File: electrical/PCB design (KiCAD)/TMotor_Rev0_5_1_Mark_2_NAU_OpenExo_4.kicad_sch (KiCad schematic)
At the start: 2 parts

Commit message: documentation update for my 10 days leave ; documentation for first time teensy setup on Arduino IDE ;  SW revamp to use HW versioning conditional compiling
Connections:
- net Left LC  Amplifier 1/Vexcitation+ renamed LEFT_AMP1_EXC
- net Left LC Amplifier 2/Vbridge+ renamed LEFT_AMP2_EXC
- net Right LC  Amplifier 2/Vexcitation+ renamed RIGHT_AMP2_EXC
- net Right LC Amplifier 1/Vexcitation+ renamed RIGHT_AMP1_EXC
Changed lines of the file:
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@@
+		)
+	)
+	(global_label "RIGHT_AMP1_EXC"
+		(shape input)
+		(at 223.52 100.33 0)
+		(fields_autoplaced yes)
+		(effects
+			(font
+				(size 1.27 1.27)
+			)
+			(justify left)
+		)
+		(property "Intersheetrefs" "${INTERSHEET_REFS}"
+			(at 242.5313 100.33 0)
+			(effects
+				(font
+					(size 1.27 1.27)
+				)
+				(justify left)
+				(hide yes)
+			)
 		)
 	)
@@
 		)
 	)
+	(global_label "LEFT_AMP1_EXC"
+		(shape input)
+		(at 120.65 88.9 0)
+		(fields_autoplaced yes)
+		(effects
+			(font
+				(size 1.27 1.27)
+			)
+			(justify left)
+		)
+		(property "Intersheetrefs" "${INTERSHEET_REFS}"
+			(at 138.4517 88.9 0)
+			(effects
+				(font
+					(size 1.27 1.27)
+				)
+				(justify left)
+				(hide yes)
+			)
+		)
+	)
+	(global_label "LEFT_AMP2_EXC"
+		(shape input)
+		(at 118.11 101.6 0)
+		(fields_autoplaced yes)
+		(effects
+			(font
+				(size 1.27 1.27)
+			)
+			(justify left)
+		)
+		(property "Intersheetrefs" "${INTERSHEET_REFS}"
+			(at 135.9117 101.6 0)
+			(effects
+				(font
+					(size 1.27 1.27)
+				)
+				(justify left)
+				(hide yes)
+			)
+		)
+	)
 	(global_label "LEFT_LC_AMP1"
 		(shape input)
@@
 				(hide yes)
 			)
+		)
+	)
+	(global_label "RIGHT_AMP2_EXC"
+		(shape input)
+		(at 223.52 81.28 0)
+		(fields_autoplaced yes)
+		(effects
+			(font
+				(size 1.27 1.27)
+			)
+			(justify left)
+		)
+		(property "Intersheetrefs" "${INTERSHEET_REFS}"
+			(at 242.5313 81.28 0)
+			(effects
+				(font
+					(size 1.27 1.27)
+				)
+				(justify left)
+				(hide yes)
+			)

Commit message: kicad update
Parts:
- added J13: TFM-107-01-L-D-WT, ISDF connector:SAMTEC_TFM-107-01-L-D-WT, symbol TFM-107-01-L-D-WT:TFM-107-01-L-D-WT
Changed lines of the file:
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@@
+	)
+	(symbol
+		(lib_id "TFM-107-01-L-D-WT:TFM-107-01-L-D-WT")
+		(at 262.89 119.38 0)
+		(unit 1)
+		(exclude_from_sim no)
+		(in_bom yes)
+		(on_board yes)
+		(dnp no)
+		(fields_autoplaced yes)
+		(property "Reference" "J13"
+			(at 262.89 104.14 0)
+			(effects
+				(font
+					(size 1.27 1.27)
+				)
+			)
+		)
+		(property "Value" "TFM-107-01-L-D-WT"
+			(at 262.89 106.68 0)
+			(effects
+				(font
+					(size 1.27 1.27)
+				)
+			)
+		)
+		(property "Footprint" "ISDF connector:SAMTEC_TFM-107-01-L-D-WT"
+			(at 262.89 119.38 0)
+			(effects
+				(font
+					(size 1.27 1.27)
+				)
+				(justify bottom)
+				(hide yes)
+			)
+		)
+		(property "Datasheet" ""
+			(at 262.89 119.38 0)
+			(effects
+				(font
+					(size 1.27 1.27)
+				)
+				(hide yes)
+			)
+		)
+		(property "Description" ""
+			(at 262.89 119.38 0)
+			(effects
+				(font
+					(size 1.27 1.27)
+				)
+				(hide yes)
+			)
+		)
+		(property "PARTREV" "T"
+			(at 262.89 119.38 0)
+			(effects
+				(font
+					(size 1.27 1.27)
+				)
+				(justify bottom)
+				(hide yes)
+			)
+		)
+		(property "MANUFACTURER" "Samtec Inc."
+			(at 262.89 119.38 0)
+			(effects
+				(font
+					(size 1.27 1.27)
+				)
+				(justify bottom)
+				(hide yes)
+			)
+		)
+		(property "MAXIMUM_PACKAGE_HEIGHT" "5.588mm"
+			(at 262.89 119.38 0)
+			(effects
+				(font
+					(size 1.27 1.27)
+				)
+				(justify bottom)
+				(hide yes)
+			)
+		)
+		(property "STANDARD" "Manufacturer Recommendations"
+			(at 262.89 119.38 0)
+			(effects
+				(font
+					(size 1.27 1.27)
+				)
+				(justify bottom)
+				(hide yes)
+			)
+		)
+		(pin "14"
+		)
+		(pin "06"
+		)
+		(pin "04"
+		)
+		(pin "10"
+		)
+		(pin "12"
+		)
+		(pin "08"
+		)
+		(pin "09"
+		)
+		(pin "07"
+		)
+		(pin "13"
+		)
+		(pin "02"
+		)
+		(pin "11"
+		)
+		(pin "03"
+		)
+		(pin "05"
+		)
+		(pin "01"
+		)
+		(instances
+			(project ""
+				(path "/3e3ff72e-d777-45cf-9299-e91389ff12dd/76f1db6b-86f9-4936-9afd-1ff77552b608"
+					(reference "J13")
+					(unit 1)
+				)
+			)
+		)
 	)
 	(symbol

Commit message: PCB version v1.1.0 design+documentation
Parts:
- removed J13: TFM-107-01-L-D-WT, ISDF connector:SAMTEC_TFM-107-01-L-D-WT, symbol TFM-107-01-L-D-WT:TFM-107-01-L-D-WT
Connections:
- net LEFT_AMP1_EXC is gone; now on net GND: LEFT_LC_CONN1.7
- net Left LC Amplifier 2/Vexcitation+ is gone; now on net Left LC Amplifier 2/Vbridge-: LEFT_LC_CONN1.3
- net RIGHT_AMP1_EXC is gone; now on net Right LC  Amplifier 2/Vbridge+: RIGHT_LC_CONN1.1
- net GND: now also LEFT_LC_CONN1.2, RIGHT_LC_CONN1.2; no longer LEFT_LC_CONN1.4, LEFT_LC_CONN1.5, RIGHT_LC_CONN1.8
- net Left LC Amplifier 2/Vbridge-: no longer LEFT_LC_CONN1.2
- net Right LC  Amplifier 2/Vbridge+: no longer RIGHT_LC_CONN1.3
- net Right LC  Amplifier 2/Vbridge-: now also RIGHT_LC_CONN1.3; no longer RIGHT_LC_CONN1.6
- net Right LC Amplifier 1/Vbridge+: now also RIGHT_LC_CONN1.8; no longer RIGHT_LC_CONN1.4
- net Right LC Amplifier 1/Vbridge-: now also RIGHT_LC_CONN1.6; no longer RIGHT_LC_CONN1.2
- net LEFT_AMP2_EXC renamed Left LC Amplifier 2/Vbridge+
- net RIGHT_AMP2_EXC renamed +5V
- net +5V: now also LEFT_LC_CONN1.4, LEFT_LC_CONN1.5, RIGHT_LC_CONN1.4
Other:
- moved on the sheet: LEFT_LC_CONN1, RIGHT_LC_CONN1

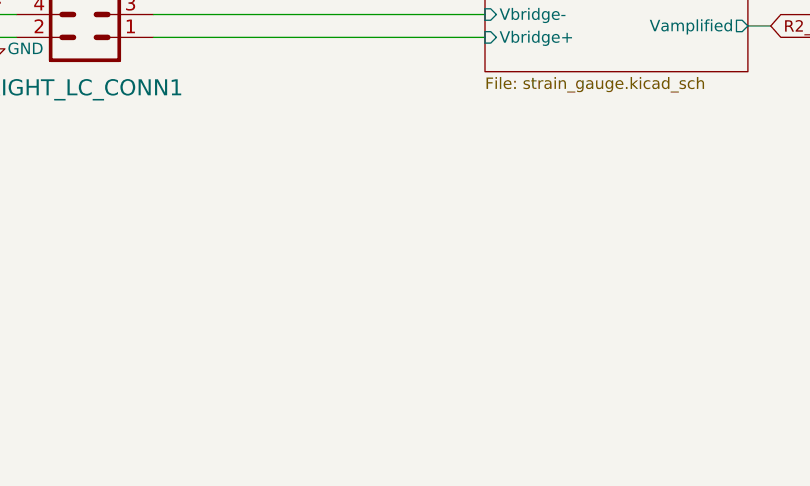
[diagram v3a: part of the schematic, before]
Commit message: Initial version for bluetooth (BLE) handler with central and peripheral implementation
Central uses Python library BLEAK and connects to the peripheral (Arduino Nano)
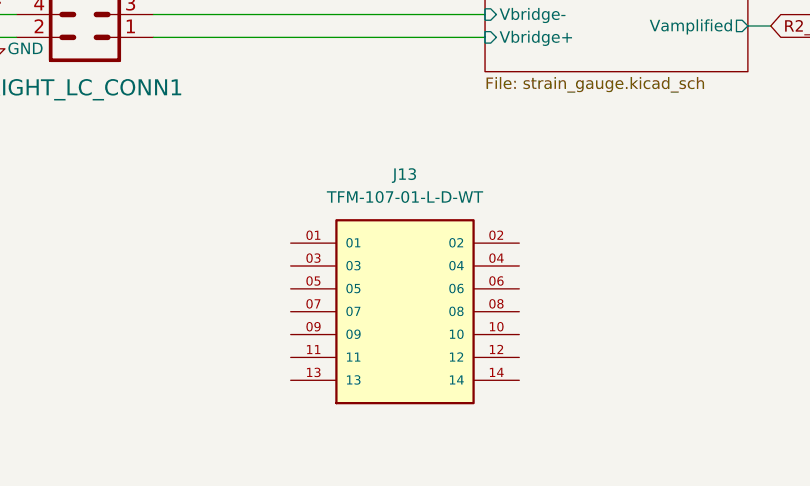
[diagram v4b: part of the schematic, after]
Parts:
- added J13: TFM-107-01-L-D-WT, ISDF connector:SAMTEC_TFM-107-01-L-D-WT, symbol TFM-107-01-L-D-WT:TFM-107-01-L-D-WT
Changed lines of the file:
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@@
+	)
+	(symbol
+		(lib_id "TFM-107-01-L-D-WT:TFM-107-01-L-D-WT")
+		(at 262.89 127 0)
+		(unit 1)
+		(exclude_from_sim no)
+		(in_bom yes)
+		(on_board yes)
+		(dnp no)
+		(fields_autoplaced yes)
+		(property "Reference" "J13"
+			(at 262.89 111.76 0)
+			(effects
+				(font
+					(size 1.27 1.27)
+				)
+			)
+		)
+		(property "Value" "TFM-107-01-L-D-WT"
+			(at 262.89 114.3 0)
+			(effects
+				(font
+					(size 1.27 1.27)
+				)
+			)
+		)
+		(property "Footprint" "ISDF connector:SAMTEC_TFM-107-01-L-D-WT"
+			(at 262.89 127 0)
+			(effects
+				(font
+					(size 1.27 1.27)
+				)
+				(justify bottom)
+				(hide yes)
+			)
+		)
+		(property "Datasheet" ""
+			(at 262.89 127 0)
+			(effects
+				(font
+					(size 1.27 1.27)
+				)
+				(hide yes)
+			)
+		)
+		(property "Description" ""
+			(at 262.89 127 0)
+			(effects
+				(font
+					(size 1.27 1.27)
+				)
+				(hide yes)
+			)
+		)
+		(property "PARTREV" "T"
+			(at 262.89 127 0)
+			(effects
+				(font
+					(size 1.27 1.27)
+				)
+				(justify bottom)
+				(hide yes)
+			)
+		)
+		(property "MANUFACTURER" "Samtec Inc."
+			(at 262.89 127 0)
+			(effects
+				(font
+					(size 1.27 1.27)
+				)
+				(justify bottom)
+				(hide yes)
+			)
+		)
+		(property "MAXIMUM_PACKAGE_HEIGHT" "5.588mm"
+			(at 262.89 127 0)
+			(effects
+				(font
+					(size 1.27 1.27)
+				)
+				(justify bottom)
+				(hide yes)
+			)
+		)
+		(property "STANDARD" "Manufacturer Recommendations"
+			(at 262.89 127 0)
+			(effects
+				(font
+					(size 1.27 1.27)
+				)
+				(justify bottom)
+				(hide yes)
+			)
+		)
+		(pin "01"
+		)
+		(pin "03"
+		)
+		(pin "05"
+		)
+		(pin "07"
+		)
+		(pin "09"
+		)
+		(pin "11"
+		)
+		(pin "13"
+		)
+		(pin "02"
+		)
+		(pin "04"
+		)
+		(pin "06"
+		)
+		(pin "08"
+		)
+		(pin "10"
+		)
+		(pin "12"
+		)
+		(pin "14"
+		)
+		(instances
+			(project ""
+				(path "/3e3ff72e-d777-45cf-9299-e91389ff12dd/76f1db6b-86f9-4936-9afd-1ff77552b608"
+					(reference "J13")
+					(unit 1)
+				)
+			)
+		)
 	)
 	(symbol

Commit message: design updates ; documentation update
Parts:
- removed LEFT_LC_CONN1, RIGHT_LC_CONN1: CONN_04X2, Connector_PinHeader_2.54mm:PinHeader_2x04_P2.54mm_Vertical, symbol TMotor_Rev0_5_1_Mark_2_NAU_OpenExo-eagle-import:CONN_04X2
- added LEFT_LC_CONN1: TFM-107-01-L-D-WT, ISDF connector:SAMTEC_TFM-107-01-L-D-WT, symbol TFM-107-01-L-D-WT:TFM-107-01-L-D-WT
- renumbered J13 to RIGHT_LC_CONN1
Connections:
- net +5V: now also RIGHT_LC_CONN1.05, RIGHT_LC_CONN1.07, LEFT_LC_CONN1.05, LEFT_LC_CONN1.07
- net GND: now also RIGHT_LC_CONN1.06, RIGHT_LC_CONN1.08, LEFT_LC_CONN1.06, LEFT_LC_CONN1.08
- net Left LC  Amplifier 1 (label 1)/Vbridge+: now also LEFT_LC_CONN1.01
- net Left LC  Amplifier 1 (label 1)/Vbridge-: now also LEFT_LC_CONN1.03
- net Left LC Amplifier 2 (label 2)/Vbridge+: now also LEFT_LC_CONN1.04
- net Left LC Amplifier 2 (label 2)/Vbridge-: now also LEFT_LC_CONN1.02
- net Right LC  Amplifier 2 (label 4)/Vbridge+: now also RIGHT_LC_CONN1.01
- net Right LC  Amplifier 2 (label 4)/Vbridge-: now also RIGHT_LC_CONN1.03
- net Right LC Amplifier 1 (label 3)/Vbridge+: now also RIGHT_LC_CONN1.04
- net Right LC Amplifier 1 (label 3)/Vbridge-: now also RIGHT_LC_CONN1.02
- no-connect marks 0 -> 12
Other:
- sheet Left LC  Amplifier 1 renamed Left LC  Amplifier 1 (label 1)
- sheet Left LC Amplifier 2 renamed Left LC Amplifier 2 (label 2)
- sheet Right LC  Amplifier 2 renamed Right LC  Amplifier 2 (label 4)
- sheet Right LC Amplifier 1 renamed Right LC Amplifier 1 (label 3)
- moved on the sheet: RIGHT_LC_CONN1

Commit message: updated ble and uart
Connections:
- net SHIELD: now reaches RIGHT_LC_CONN1.14
- net SHIELD: now also LEFT_LC_CONN1.14
- no-connect marks 12 -> 10
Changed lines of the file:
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@@
-	)
-	(no_connect
-		(at 245.11 104.14)
 	)
 	(no_connect
@@
 	)
 	(no_connect
-		(at 125.73 143.51)
-	)
-	(no_connect
 		(at 100.33 140.97)
 	)
@@
 	(wire
 		(pts
+			(xy 125.73 143.51) (xy 125.73 146.05)
+		)
+		(stroke
+			(width 0)
+			(type default)
+		)
+	)
+	(wire
+		(pts
 			(xy 214.63 96.52) (xy 219.71 96.52)
+		)
+		(stroke
+			(width 0)
+			(type default)
+		)
+	)
+	(wire
+		(pts
+			(xy 245.11 104.14) (xy 245.11 106.68)
 		)
 		(stroke
@@
 					(unit 1)
 				)
+			)
+		)
+	)
+	(symbol
+		(lib_id "power:GND")
+		(at 125.73 146.05 0)
+		(unit 1)
+		(exclude_from_sim no)
+		(in_bom yes)
+		(on_board yes)
+		(dnp no)
+		(fields_autoplaced yes)
+		(property "Reference" "#PWR062"
+			(at 125.73 152.4 0)
+			(effects
+				(font
+					(size 1.27 1.27)
+				)
+				(hide yes)
+			)
+		)
+		(property "Value" "SHIELD"
+			(at 125.73 151.13 0)
+			(effects
+				(font
+					(size 1.27 1.27)
+				)
+			)
+		)
+		(property "Footprint" ""
+			(at 125.73 146.05 0)
+			(effects
+				(font
+					(size 1.27 1.27)
+				)
+				(hide yes)
+			)
+		)
+		(property "Datasheet" ""
+			(at 125.73 146.05 0)
+			(effects
+				(font
+					(size 1.27 1.27)
+				)
+				(hide yes)
+			)
+		)
+		(property "Description" "Power symbol creates a global label with name \"GND\" , ground"
+			(at 125.73 146.05 0)
+			(effects
+				(font
+					(size 1.27 1.27)
+				)
+				(hide yes)
+			)
+		)
+		(pin "1"
+		)
+		(instances
+			(project "TMotor_Rev0_5_1_Mark_2_NAU_OpenExo"
+				(path "/3e3ff72e-d777-45cf-9299-e91389ff12dd/76f1db6b-86f9-4936-9afd-1ff77552b608"
+					(reference "#PWR062")
+					(unit 1)
+				)
+			)
+		)
+	)
+	(symbol
+		(lib_id "power:GND")
+		(at 245.11 106.68 0)
+		(unit 1)
+		(exclude_from_sim no)
+		(in_bom yes)
+		(on_board yes)
+		(dnp no)
+		(fields_autoplaced yes)
+		(property "Reference" "#PWR052"
+			(at 245.11 113.03 0)
+			(effects
+				(font
+					(size 1.27 1.27)
+				)
+				(hide yes)
+			)
+		)
+		(property "Value" "SHIELD"
+			(at 245.11 111.76 0)
+			(effects
+				(font
+					(size 1.27 1.27)
+				)
+			)
+		)
+		(property "Footprint" ""
+			(at 245.11 106.68 0)
+			(effects
+				(font
+					(size 1.27 1.27)
+				)
+				(hide yes)
+			)
+		)
+		(property "Datasheet" ""
+			(at 245.11 106.68 0)
+			(effects
+				(font
+					(size 1.27 1.27)
+				)
+				(hide yes)
+			)
+		)
+		(property "Description" "Power symbol creates a global label with name \"GND\" , ground"
+			(at 245.11 106.68 0)
+			(effects
+				(font
+					(size 1.27 1.27)
+				)
+				(hide yes)
+			)
+		)
+		(pin "1"
+		)
+		(instances
+			(project "TMotor_Rev0_5_1_Mark_2_NAU_OpenExo"
+				(path "/3e3ff72e-d777-45cf-9299-e91389ff12dd/76f1db6b-86f9-4936-9afd-1ff77552b608"
+					(reference "#PWR052")
+					(unit 1)
+				)

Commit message: fix modularize python script for ble.py and sensors.py (main and plotting-csv not done
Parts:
- added JP1, JP2: SolderJumper_3_Open, Jumper:SolderJumper-3_P1.3mm_Open_RoundedPad1.0x1.5mm, symbol Jumper:SolderJumper_3_Open
- LEFT_LC_CONN1, RIGHT_LC_CONN1: footprint ISDF connector:SAMTEC_TFM-107-01-L-D-WT -> TFM-107-01-L-D-WT:SAMTEC_TFM-107-01-L-D-WT
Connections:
- net +5V: now also JP1.1 (A), JP2.1 (A)
- net SHIELD: now also LEFT_LC_CONN1.S1, LEFT_LC_CONN1.S2, RIGHT_LC_CONN1.S1, RIGHT_LC_CONN1.S2
- net FSR1/Vexcitation: now reaches RIGHT_LC_CONN1.10
- net FSR2/Vfsr: now reaches RIGHT_LC_CONN1.11
- net FSR1/Vfsr: now reaches RIGHT_LC_CONN1.12
- net FSR2/Vexcitation: now reaches RIGHT_LC_CONN1.13
- new net +3V3: JP1.3 (B), JP2.3 (B)
- new net FSR1/Vin: JP2.2 (C)
- new net FSR2/Vin: JP1.2 (C)
- no-connect marks 10 -> 6
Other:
- added sheet FSR1 (FSR.kicad_sch)
- added sheet FSR2 (FSR.kicad_sch)
